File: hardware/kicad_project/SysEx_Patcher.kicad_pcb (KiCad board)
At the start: 4 copper layers, 172 x 172 mm, 95 parts, among them J1 MIDI_IN, J10 JACK6.35, J2 MIDI_OUT, J3 DC_5V, J4 BAT_PWR, J5 OLED, SW2 SW, SW3 SW, SW4 SW, SW5 SW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

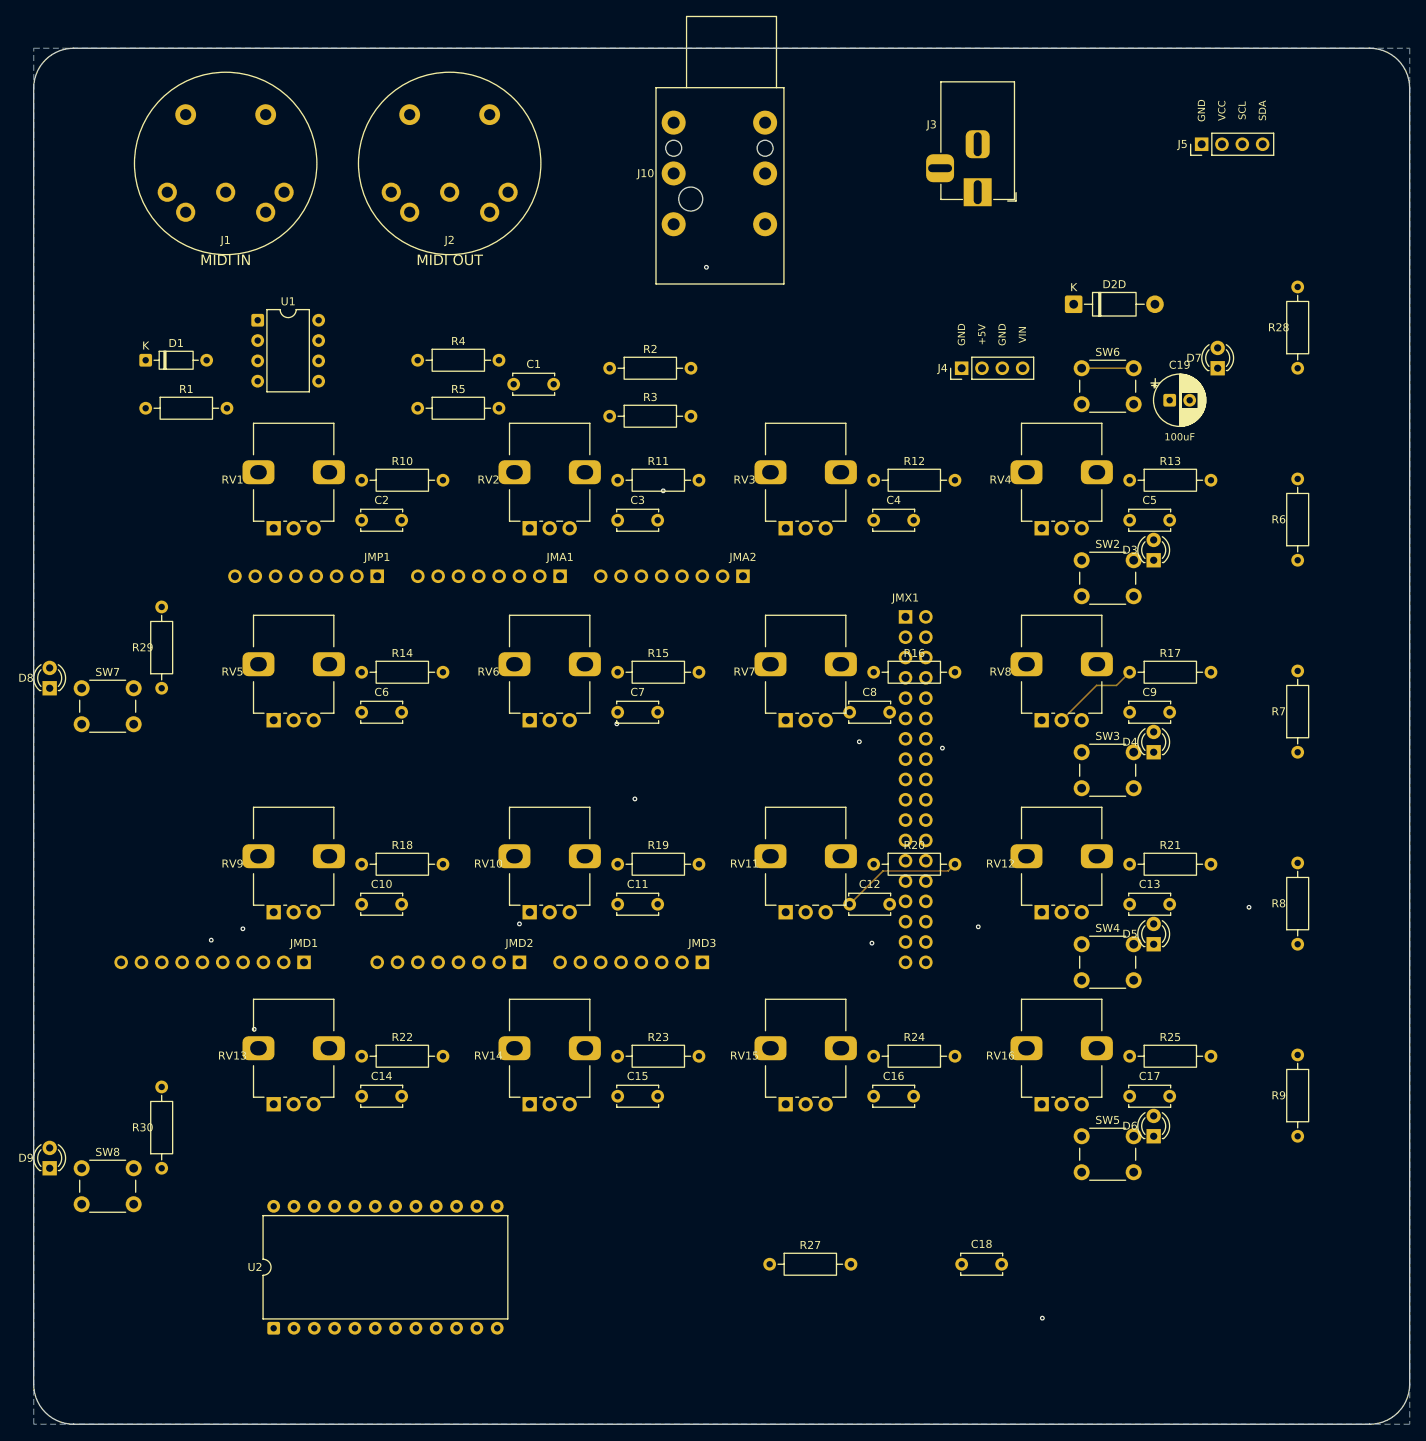
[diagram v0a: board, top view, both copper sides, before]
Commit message: shield: D8/D9 à droite des boutons + SW2-5 écartés des pots ; re-route 100% (0 net restant)
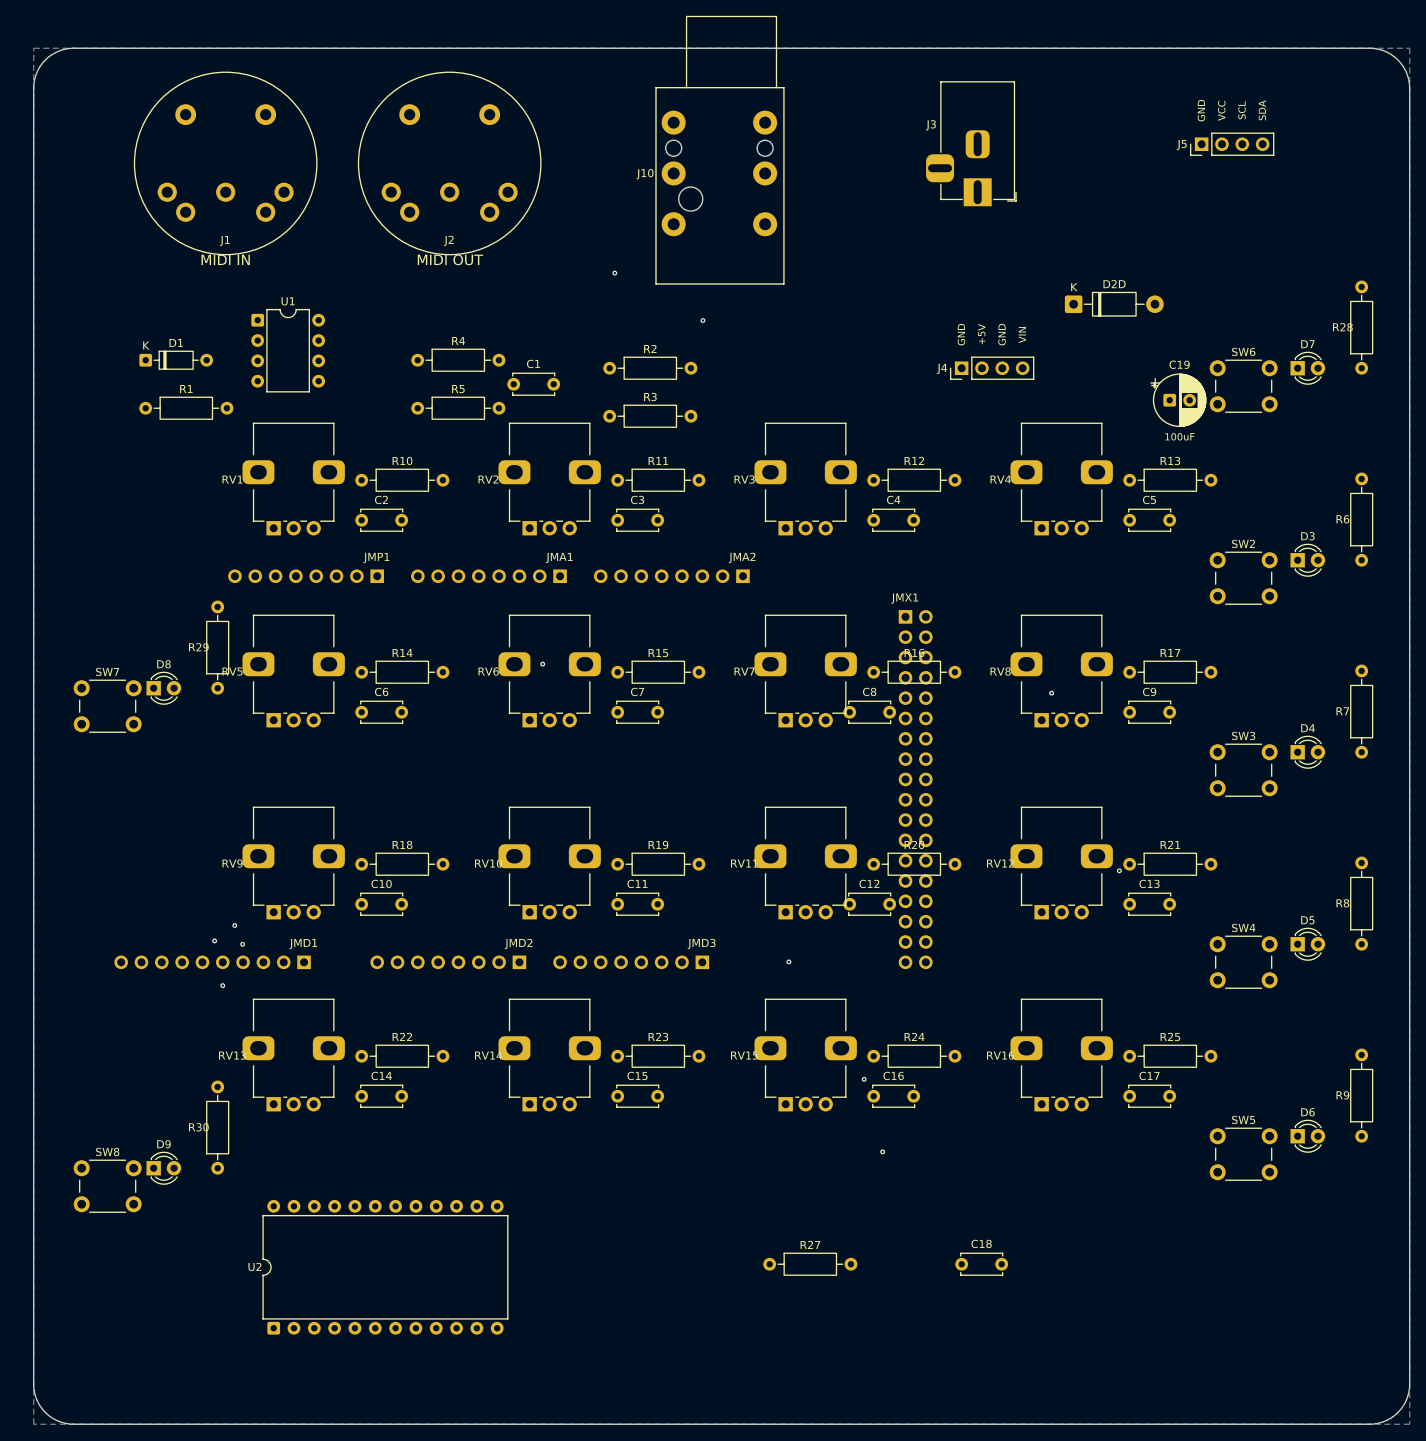
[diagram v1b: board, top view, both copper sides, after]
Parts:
- moved D3 18.0 mm to (178.0, 84.0), turned to 0 degrees
- moved D4 18.0 mm to (178.0, 108.0), turned to 0 degrees
- moved D5 18.0 mm to (178.0, 132.0), turned to 0 degrees
- moved D6 18.0 mm to (178.0, 156.0), turned to 0 degrees
- moved SW2 17.0 mm to (168.0, 84.0)
- moved SW3 17.0 mm to (168.0, 108.0)
- moved SW4 17.0 mm to (168.0, 132.0)
- moved SW5 17.0 mm to (168.0, 156.0)
- moved SW6 17.0 mm to (168.0, 60.0)
- moved D8 13.0 mm to (35.0, 100.0), turned to 0 degrees
- moved D9 13.0 mm to (35.0, 160.0), turned to 0 degrees
- moved D7 10.0 mm to (178.0, 60.0), turned to 0 degrees
- moved R28 8.00 mm to (186.0, 60.0)
- moved R6 8.00 mm to (186.0, 84.0)
- moved R7 8.00 mm to (186.0, 108.0)
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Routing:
- net A7: track 12.2 -> 92.1 mm, vias 0 -> 1
- net D21_SCL: track 197.1 -> 216.7 mm
- net D6: track 81.7 -> 99.1 mm
- net D8: track 137.4 -> 154.4 mm
- net D5: track 90.9 -> 107.9 mm
- net D26: track 126.3 -> 141.4 mm
- net A6: track 72.3 -> 59.6 mm, vias 1 -> 0
- net D9: track 154.6 -> 164.7 mm
- net MUX_CH0: track 120.8 -> 110.9 mm, vias 1 -> 0
- net LED3_A: track 21.3 -> 12.4 mm
- net LED4_A: track 21.2 -> 12.4 mm
- net LED2_A: track 21.2 -> 12.4 mm
- net LED1_A: track 21.2 -> 12.4 mm
- net +5V: track 640.1 -> 631.3 mm, vias 0 -> 1
- net D10: track 148.3 -> 156.9 mm, vias 1 -> 0
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
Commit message: shield: fix miroir (transformation propre, s'enfiche vraiment) + sérigraphie des embases Mega + re-route + Gerbers
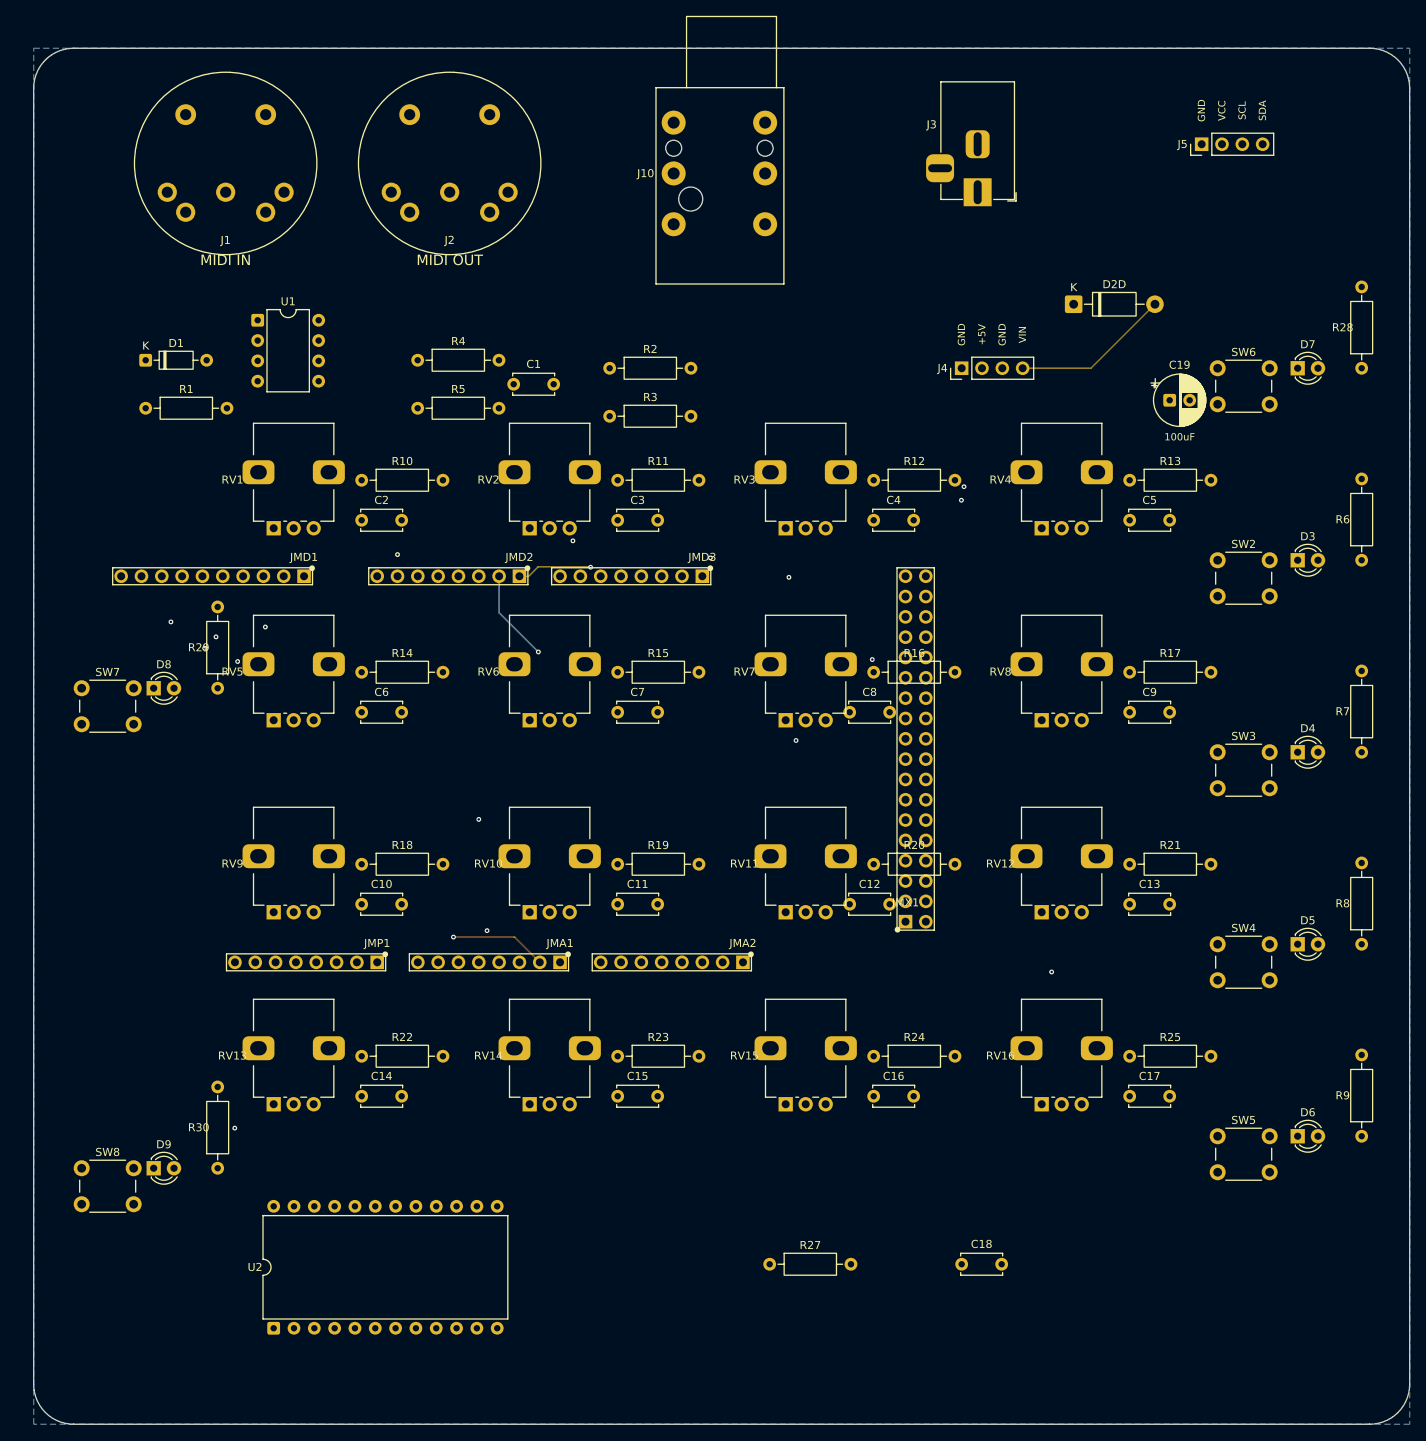
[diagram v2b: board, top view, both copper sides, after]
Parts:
- moved JMA1 48.3 mm to (85.8, 134.3)
- moved JMA2 48.3 mm to (108.7, 134.3)
- moved JMD1 48.3 mm to (53.8, 86.0)
- moved JMD2 48.3 mm to (80.7, 86.0)
- moved JMD3 48.3 mm to (103.6, 86.0)
- moved JMP1 48.3 mm to (62.9, 134.3)
- moved JMX1 38.1 mm to (129.0, 129.2)
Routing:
- net D21_SCL: track 216.7 -> 142.3 mm
- net D20_SDA: track 205.2 -> 146.3 mm, vias 1 -> 0
- net A3: track 84.3 -> 26.9 mm
- net D13: track 56.6 -> 108.4 mm
- net D4: track 31.5 -> 82.3 mm
- net A0: track 32.0 -> 81.8 mm, vias 0 -> 1
- net D5: track 107.9 -> 157.3 mm, vias 0 -> 1
- net D2: track 47.7 -> 97.0 mm
- net D3: track 47.7 -> 97.0 mm
- net D0_RX: track 86.2 -> 37.9 mm
- net A7: track 92.1 -> 44.1 mm, vias 1 -> 0
- net A12: track 73.6 -> 120.3 mm, vias 0 -> 1
- net A11: track 87.2 -> 43.1 mm
- net A5: track 35.0 -> 78.6 mm
- net A8: track 31.5 -> 74.3 mm
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
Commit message: shield: dégage R16/R20 (filtres pots) du 2x18, passe en vertical ; re-route 100% + Gerbers
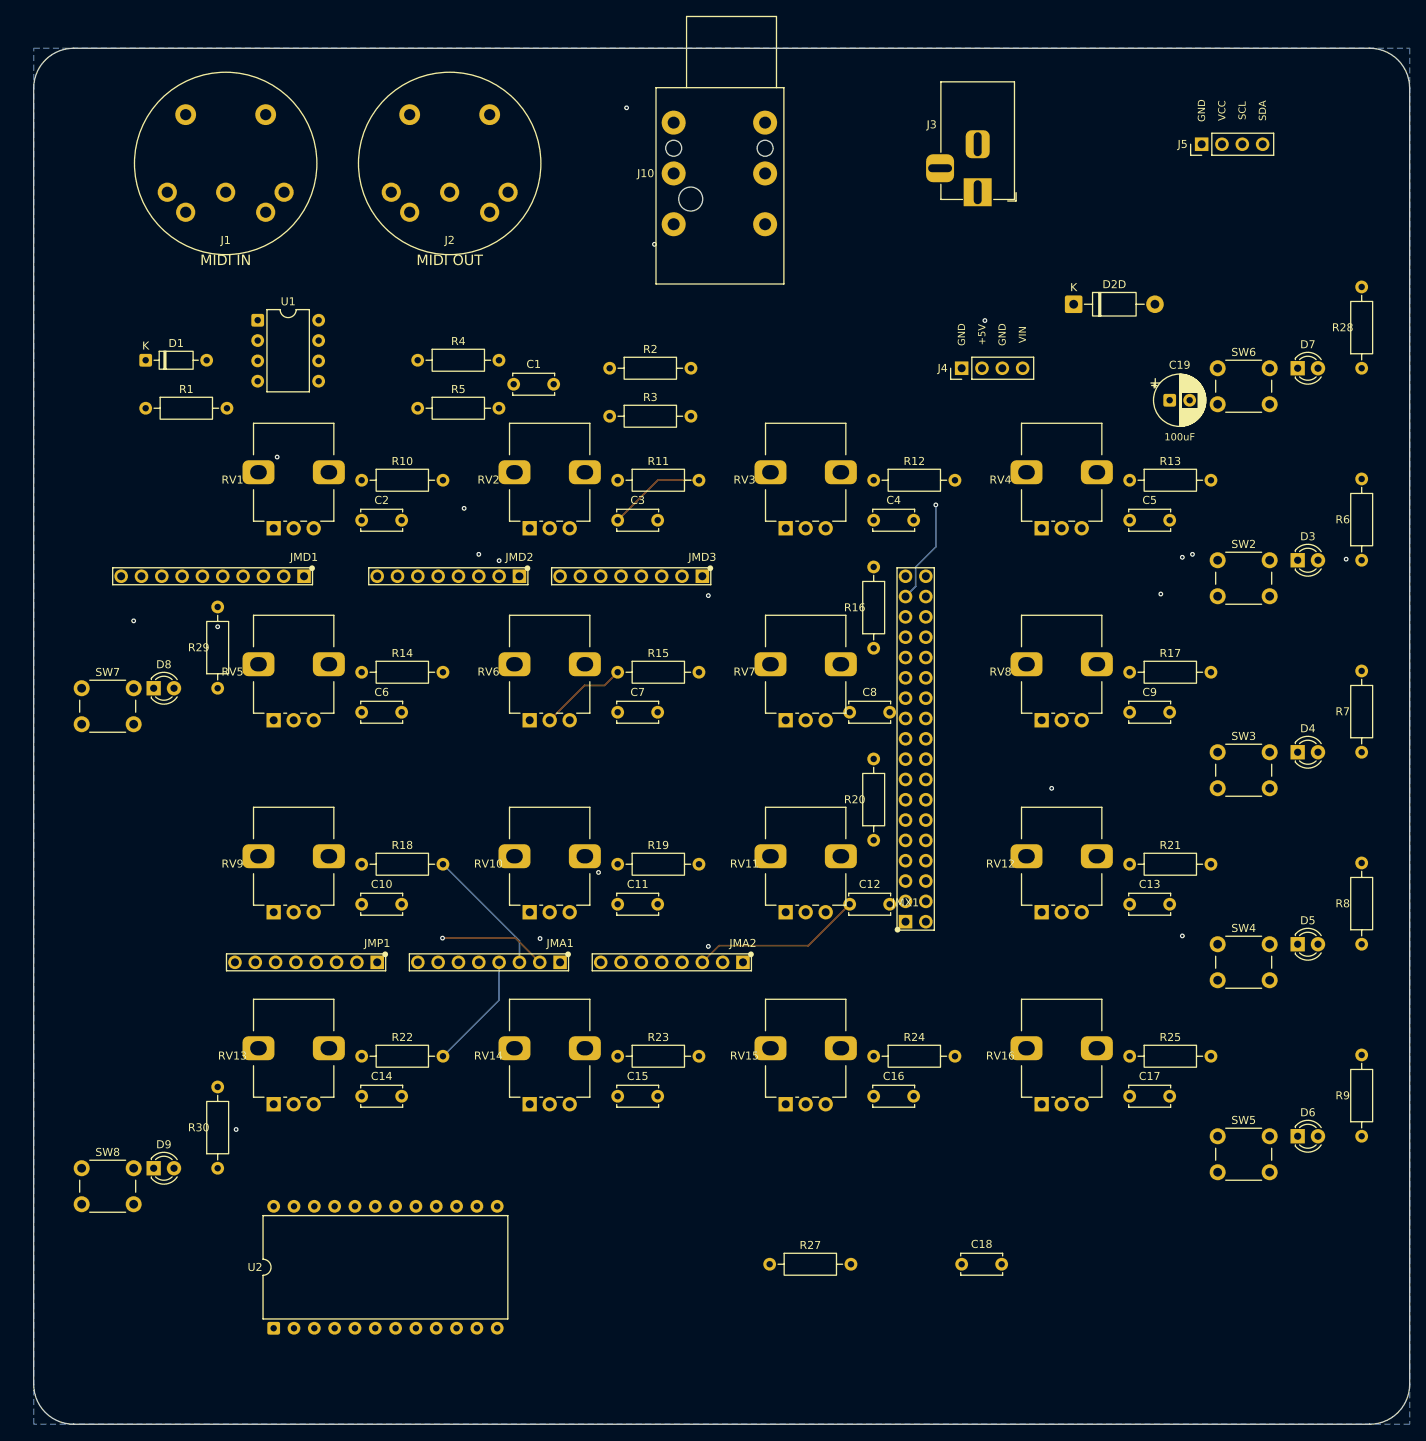
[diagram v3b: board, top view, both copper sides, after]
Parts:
- moved R16 3.00 mm to (125.0, 95.0), turned to 90 degrees
- moved R20 3.00 mm to (125.0, 119.0), turned to 90 degrees
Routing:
- net D9: track 192.5 -> 229.4 mm, vias 0 -> 1
- net D27: track 154.1 -> 119.3 mm, vias 2 -> 0
- net D26: track 163.4 -> 130.5 mm, vias 1 -> 0
- net D21_SCL: track 142.3 -> 173.8 mm
- net D6: track 119.6 -> 146.5 mm, vias 1 -> 3
- net D10: track 172.1 -> 195.8 mm, vias 1 -> 2
- net D20_SDA: track 146.3 -> 164.9 mm, vias 0 -> 1
- net VIN_RAW: track 188.6 -> 205.1 mm, vias 1 -> 2
- net A13: track 102.0 -> 86.2 mm, vias 1 -> 0
- net D5: track 157.3 -> 172.9 mm, vias 1 -> 2
- net A12: track 120.3 -> 107.5 mm
- net A7: track 44.1 -> 52.2 mm
- net A4: track 53.2 -> 60.5 mm, vias 0 -> 1
- net POT11_W: track 11.0 -> 17.1 mm
- net A2: track 34.4 -> 28.5 mm
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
